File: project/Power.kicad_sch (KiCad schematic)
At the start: 20 parts

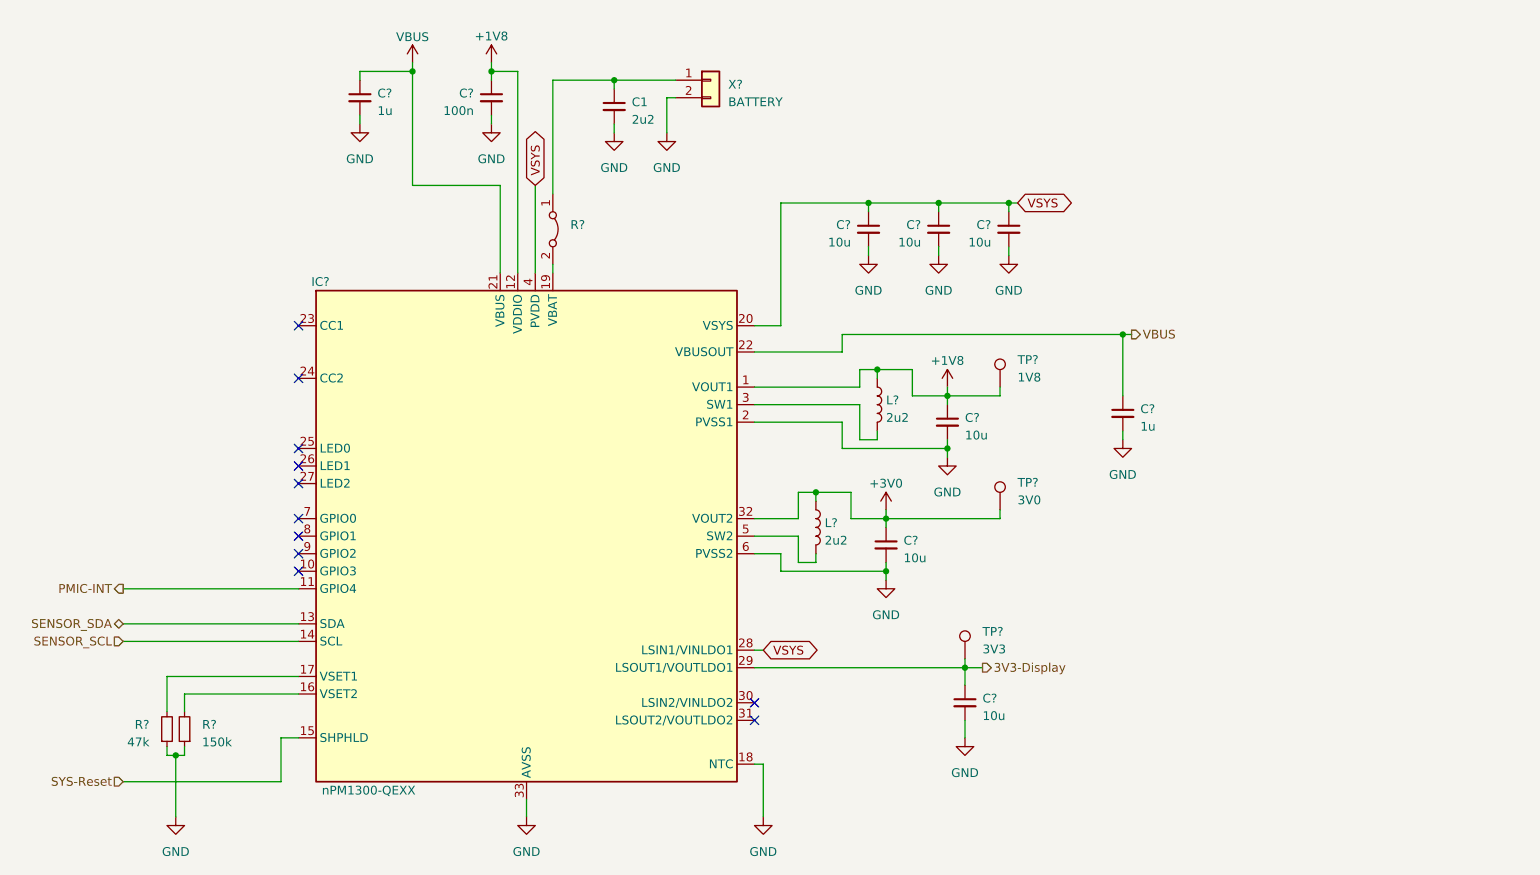
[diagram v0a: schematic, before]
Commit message: - Add QR code library with link to the project - Change ISET resistor to 12k - Replace light sensor footprint with a version from our KiCad library - Rename the inner copper layers - Add KiBot file for production file generation - Import nPM1300 from test project - Remove pull down resistor from vibration driver IC enable - Split schematics into hierarical schematics - Add PCB variant for reduced sensor board - Add I2S microphone - Update all symbols and footprints
Signed-off-by: Daniel Kampert <DanielKampert@kampis-elektroecke.de>
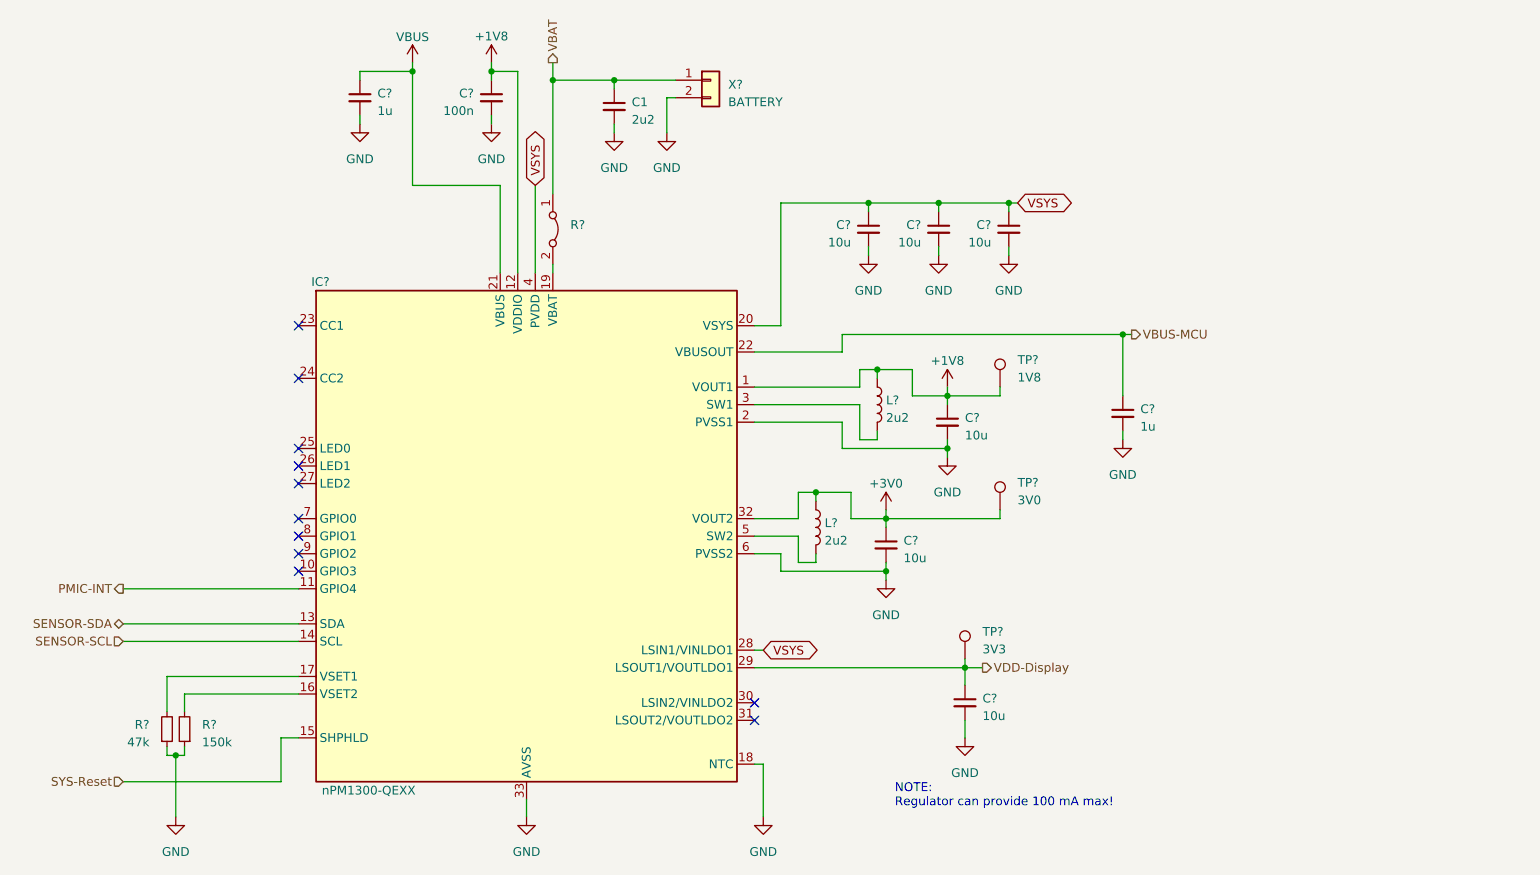
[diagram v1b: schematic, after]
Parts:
- TP? (x3): footprint TestPoint:TestPoint_Pad_1.0x1.0mm -> TestPoint:TestPoint_Pad_D1.0mm
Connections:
- net VBUS: no longer C?.1, IC?.22 (VBUSOUT)
- net VBAT: now reaches C1.1, R?.1 (A), X?.1 (Pin_1)
- net 3V3-Display renamed VDD-Display
- net SENSOR_SCL renamed SENSOR-SCL
- net SENSOR_SDA renamed SENSOR-SDA
- new net VBUS-MCU: C?.1, IC?.22 (VBUSOUT)
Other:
- note added: "NOTE: Regulator can provide 100 mA max!"
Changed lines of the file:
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@@
   (title_block
     (title "ZSWatch v2")
-    (date "2023-11-28")
-    (rev "5")
+    (date "2023-11-29")
+    (rev "5-Draft")
     (company "github.com/jakkra/ZSWatch-HW")
   )
   (junction (at 181.61 59.69) (diameter 0) (color 0 0 0 0)
+  )
+  (junction (at 135.89 41.91) (diameter 0) (color 0 0 0 0)
   )
   (junction (at 182.88 83.82) (diameter 0) (color 0 0 0 0)
@@
     (stroke (width 0) (type default))
   )
+  (wire (pts (xy 135.89 39.37) (xy 135.89 41.91))
+    (stroke (width 0) (type default))
+  )
   (wire (pts (xy 182.88 83.82) (xy 187.96 83.82))
     (stroke (width 0) (type default))
@@
   (wire (pts (xy 133.35 69.85) (xy 133.35 57.15))
     (stroke (width 0) (type default))
+  )
+  (text "NOTE:\nRegulator can provide 100 mA max!" (at 185.42 147.32 0)
+    (effects (font (size 1.27 1.27)) (justify left bottom))
   )
   (global_label "VSYS" (shape bidirectional) (at 166.37 124.46 0) (fields_autoplaced)
@@
     )
   )
-  (hierarchical_label "VBUS" (shape output) (at 219.71 78.74 0) (fields_autoplaced)
+  (hierarchical_label "VBUS-MCU" (shape output) (at 219.71 78.74 0) (fields_autoplaced)
     (effects (font (size 1.27 1.27)) (justify left))
   )
-  (hierarchical_label "SENSOR_SCL" (shape input) (at 73.66 123.19 180) (fields_autoplaced)
+  (hierarchical_label "SENSOR-SCL" (shape input) (at 73.66 123.19 180) (fields_autoplaced)
     (effects (font (size 1.27 1.27)) (justify right))
   )
-  (hierarchical_label "SENSOR_SDA" (shape bidirectional) (at 73.66 120.65 180) (fields_autoplaced)
+  (hierarchical_label "SENSOR-SDA" (shape bidirectional) (at 73.66 120.65 180) (fields_autoplaced)
     (effects (font (size 1.27 1.27)) (justify right))
   )
-  (hierarchical_label "3V3-Display" (shape output) (at 198.12 127 0) (fields_autoplaced)
+  (hierarchical_label "VDD-Display" (shape output) (at 198.12 127 0) (fields_autoplaced)
     (effects (font (size 1.27 1.27)) (justify left))
   )
@@
     (effects (font (size 1.27 1.27)) (justify right))
   )
+  (hierarchical_label "VBAT" (shape output) (at 135.89 39.37 90) (fields_autoplaced)
+    (effects (font (size 1.27 1.27)) (justify left))
+  )
   (hierarchical_label "PMIC-INT" (shape output) (at 73.66 115.57 180) (fields_autoplaced)
     (effects (font (size 1.27 1.27)) (justify right))
@@
       (effects (font (size 1.27 1.27)) hide)
     )
-    (property "Datasheet" "https://www.mouser.de/datasheet/2/40/KGM_X7R-3223212.pdf" (at 218.44 90.17 0)
+    (property "Datasheet" "~" (at 218.44 90.17 0)
       (effects (font (size 1.27 1.27)) hide)
     )
@@
       (effects (font (size 1.27 1.27)) hide)
     )
-    (property "Datasheet" "https://www.mouser.de/datasheet/2/585/sems_s_a0006918008_1-2288745.pdf" (at 173.99 106.68 0)
+    (property "Datasheet" "~" (at 173.99 106.68 0)
       (effects (font (size 1.27 1.27)) hide)
     )
@@
       (effects (font (size 1.27 1.27)) hide)
     )
-    (property "Datasheet" "https://www.mouser.de/datasheet/2/40/KGM_X7R-3223212.pdf" (at 107.95 44.45 0)
+    (property "Datasheet" "~" (at 107.95 44.45 0)
       (effects (font (size 1.27 1.27)) hide)
     )
@@
       (effects (font (size 1.27 1.27)) hide)
     )
-    (property "Datasheet" "https://www.mouser.de/datasheet/2/40/CM_Series_e-2835982.pdf" (at 184.15 109.22 0)
+    (property "Datasheet" "~" (at 184.15 109.22 0)
       (effects (font (size 1.27 1.27)) hide)
     )
@@
       (effects (font (size 1.27 1.27)) hide)
     )
-    (property "Datasheet" "https://www.mouser.de/datasheet/2/447/YAGEO_PYu_RC_Group_51_RoHS_L_12-3313492.pdf" (at 82.55 135.89 0)
+    (property "Datasheet" "~" (at 82.55 135.89 0)
       (effects (font (size 1.27 1.27)) hide)
     )
@@
       (effects (font (size 1.27 1.27)) (justify left))
     )
-    (property "Footprint" "TestPoint:TestPoint_Pad_1.0x1.0mm" (at 200.66 125.73 0)
+    (property "Footprint" "TestPoint:TestPoint_Pad_D1.0mm" (at 200.66 125.73 0)
       (effects (font (size 1.27 1.27)) hide)
     )
@@
       (effects (font (size 1.27 1.27)) hide)
     )
-    (property "Datasheet" "https://www.mouser.de/datasheet/2/40/CM_Series_e-2835982.pdf" (at 193.04 91.44 0)
+    (property "Datasheet" "~" (at 193.04 91.44 0)
       (effects (font (size 1.27 1.27)) hide)
     )
@@
       (effects (font (size 1.27 1.27)) hide)
     )
-    (property "Datasheet" "https://www.mouser.de/datasheet/2/447/YAGEO_PYu_RC_Group_51_RoHS_L_12-3313492.pdf" (at 80.01 135.89 0)
+    (property "Datasheet" "~" (at 80.01 135.89 0)
       (effects (font (size 1.27 1.27)) hide)
     )
@@
     (pin "18")
     (pin "19")
+    (pin "2")
+    (pin "20")
     (pin "21")
+    (pin "22")
     (pin "23")
     (pin "24")
@@
     (pin "26")
     (pin "27")
+    (pin "28")
     (pin "29")
     (pin "3")
@@
     (pin "4")
     (pin "5")
+    (pin "6")
     (pin "7")
     (pin "8")
     (pin "9")
-    (pin "2")
-    (pin "20")
-    (pin "22")
-    (pin "28")
-    (pin "6")
     (instances
       (project "ZSWatch"
@@
       (effects (font (size 1.27 1.27)) hide)
     )
-    (property "Datasheet" "https://www.mouser.de/datasheet/2/40/CM_Series_e-2835982.pdf" (at 191.77 63.5 0)
+    (property "Datasheet" "~" (at 191.77 63.5 0)
       (effects (font (size 1.27 1.27)) hide)
     )
@@
       (effects (font (size 1.27 1.27)) hide)
     )
-    (property "Datasheet" "https://www.mouser.de/datasheet/2/585/sems_s_a0006918008_1-2288745.pdf" (at 182.88 88.9 0)
+    (property "Datasheet" "~" (at 182.88 88.9 0)
       (effects (font (size 1.27 1.27)) hide)
     )
@@
       (effects (font (size 1.27 1.27)) hide)
     )
-    (property "Datasheet" "https://tools.molex.com/pdm_docs/sd/781710002_sd.pdf" (at 158.75 41.91 0)
+    (property "Datasheet" "~" (at 158.75 41.91 0)
       (effects (font (size 1.27 1.27)) hide)
     )
@@
       (effects (font (size 1.27 1.27)) hide)
     )
-    (property "Datasheet" "https://www.mouser.de/datasheet/2/40/CM_Series_e-2835982.pdf" (at 181.61 63.5 0)
+    (property "Datasheet" "~" (at 181.61 63.5 0)
       (effects (font (size 1.27 1.27)) hide)
     )
@@
       (effects (font (size 1.27 1.27)) hide)
     )
-    (property "Datasheet" "https://www.mouser.de/datasheet/2/40/KGM_X7R-3223212.pdf" (at 144.78 45.72 0)
+    (property "Datasheet" "~" (at 144.78 45.72 0)
       (effects (font (size 1.27 1.27)) hide)
     )
@@
       (effects (font (size 1.27 1.27)) hide)
     )
-    (property "Datasheet" "https://www.mouser.de/datasheet/2/40/CM_Series_e-2835982.pdf" (at 195.58 132.08 0)
+    (property "Datasheet" "~" (at 195.58 132.08 0)
       (effects (font (size 1.27 1.27)) hide)
     )
@@
       (effects (font (size 1.27 1.27)) (justify left))
     )
-    (property "Footprint" "TestPoint:TestPoint_Pad_1.0x1.0mm" (at 205.74 104.14 0)
+    (property "Footprint" "TestPoint:TestPoint_Pad_D1.0mm" (at 205.74 104.14 0)
       (effects (font (size 1.27 1.27)) hide)
     )
@@
       (effects (font (size 1.27 1.27)) hide)
     )
-    (property "Datasheet" "https://www.mouser.de/datasheet/2/40/KGM_X7R-3223212.pdf" (at 127 44.45 0)
+    (property "Datasheet" "~" (at 127 44.45 0)
       (effects (font (size 1.27 1.27)) hide)
     )
@@
       (effects (font (size 1.27 1.27)) hide)
     )
-    (property "Datasheet" "https://www.mouser.de/datasheet/2/40/CM_Series_e-2835982.pdf" (at 201.93 63.5 0)
+    (property "Datasheet" "~" (at 201.93 63.5 0)
       (effects (font (size 1.27 1.27)) hide)
     )
@@
       (effects (font (size 1.27 1.27)) (justify left))
     )
-    (property "Footprint" "TestPoint:TestPoint_Pad_1.0x1.0mm" (at 205.74 86.36 0)
-      (effects (font (size 1.27 1.27)) hide)
-    )
+    (property "Footprint" "TestPoint:TestPoint_Pad_D1.0mm" (at 205.74 86.36 0)
+      (effects (font (size 1.27 1.27)) hide)
+    )

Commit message: - Add QR code library with link to the project - Change ISET resistor to 12k - Replace light sensor footprint with a version from our KiCad library - Rename the inner copper layers - Add KiBot file for production file generation - Import nPM1300 from test project - Remove pull down resistor from vibration driver IC enable - Split schematics into hierarical schematics - Add PCB variant for reduced sensor board - Add I2S microphone - Update all symbols and footprints - Move BTN_2 from P0.30 to P1.10 - Move BTN_3 from P1.12 to P0.31 - Move DRV_VIB_EN from P1.14 to P1.05 - Move BMI270_IN1 from P0.21 to P1.08 - Move BMI270_IN2 from P0.19 to P1.04 - Move DRV_VIB_PWM from P1.15 to P1.05 - Move DRV_VIB_EN from P1.05 to P1.15 - Move BTN_4 from P1.06 to P0.26 - Replace ESDALC6V1W5 with ESDALC6V1P5 - Add USB support (experimental) - Add marker for display cable orientation - Add markers for better IC placements - Replace the flash memory with WSON-8 variant to allow 64 MB devices - Remove old PCBWay documentation
Signed-off-by: Daniel Kampert <DanielKampert@kampis-elektroecke.de>
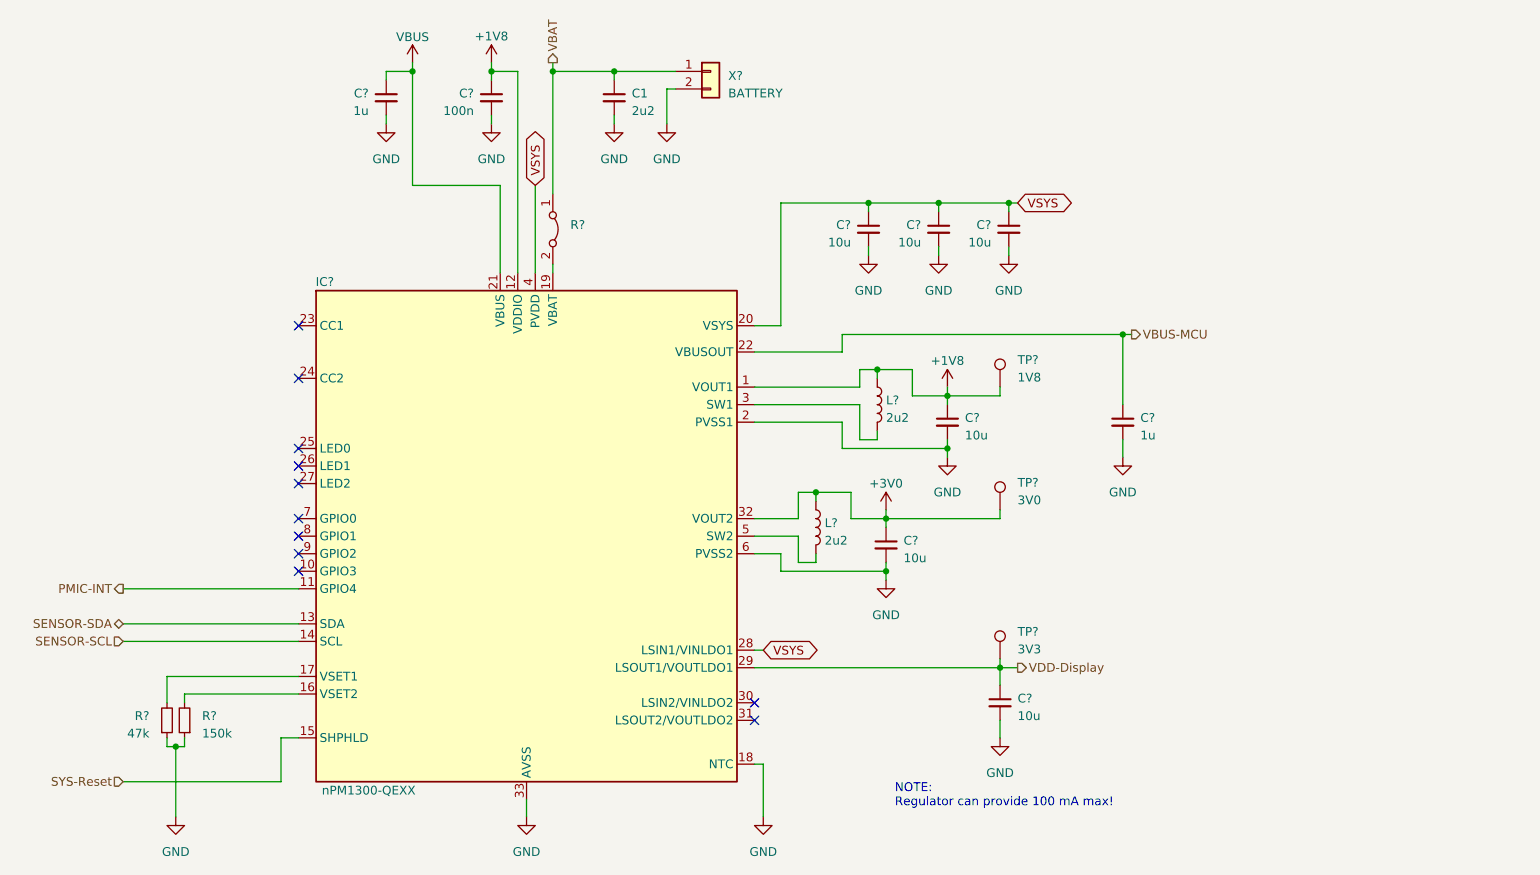
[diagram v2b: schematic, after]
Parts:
- R?: now left out of the parts list
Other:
- moved on the sheet: C1, C?, R?, TP?, X?

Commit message: - Remove S1, S2 and S4 from Sensor variant - Remove microphone from Sensor variant - Update symbols - Add missing supply chain documentation - Update KiBot template to the newest version
Signed-off-by: Daniel Kampert <DanielKampert@kampis-elektroecke.de>
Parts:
- R?: Mfr. No. (none) -> RC0603FR-07150KL; Order Number (none) -> 603-RC0603FR-07150KL
- R?: Mfr. No. (none) -> RC0603FR-0747KL; Order Number (none) -> 603-RC0603FR-0747KL
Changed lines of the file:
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@@
       (effects (font (size 1.27 1.27)) hide)
     )
-    (property "Datasheet" "https://product.samsungsem.com/pi/CIGT201610EH2R2MN.do" (at 173.99 106.68 0)
+    (property "Datasheet" "~" (at 173.99 106.68 0)
       (effects (font (size 1.27 1.27)) hide)
     )
@@
       (effects (font (size 1.27 1.27)) hide)
     )
-    (property "Mfr. No." "" (at 82.55 134.62 0)
-      (effects (font (size 1.27 1.27)) hide)
-    )
-    (property "Order Number" "" (at 82.55 134.62 0)
+    (property "Mfr. No." "RC0603FR-07150KL" (at 82.55 134.62 0)
+      (effects (font (size 1.27 1.27)) hide)
+    )
+    (property "Order Number" "603-RC0603FR-07150KL" (at 82.55 134.62 0)
       (effects (font (size 1.27 1.27)) hide)
     )
@@
       (effects (font (size 1.27 1.27)) hide)
     )
-    (property "Mfr. No." "" (at 80.01 134.62 0)
-      (effects (font (size 1.27 1.27)) hide)
-    )
-    (property "Order Number" "" (at 80.01 134.62 0)
+    (property "Mfr. No." "RC0603FR-0747KL" (at 80.01 134.62 0)
+      (effects (font (size 1.27 1.27)) hide)
+    )
+    (property "Order Number" "603-RC0603FR-0747KL" (at 80.01 134.62 0)
       (effects (font (size 1.27 1.27)) hide)
     )
@@
       (effects (font (size 1.27 1.27)) hide)
     )
-    (property "Datasheet" "https://product.samsungsem.com/pi/CIGT201610EH2R2MN.do" (at 182.88 88.9 0)
-      (effects (font (size 1.27 1.27)) hide)
-    )
+    (property "Datasheet" "~" (at 182.88 88.9 0)
+      (effects (font (size 1.27 1.27)) hide)
+    )
